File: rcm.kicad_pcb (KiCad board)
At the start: 2 copper layers, 140 x 70 mm, 159 parts, among them Y1 8MHz, Y2 32.768kHz

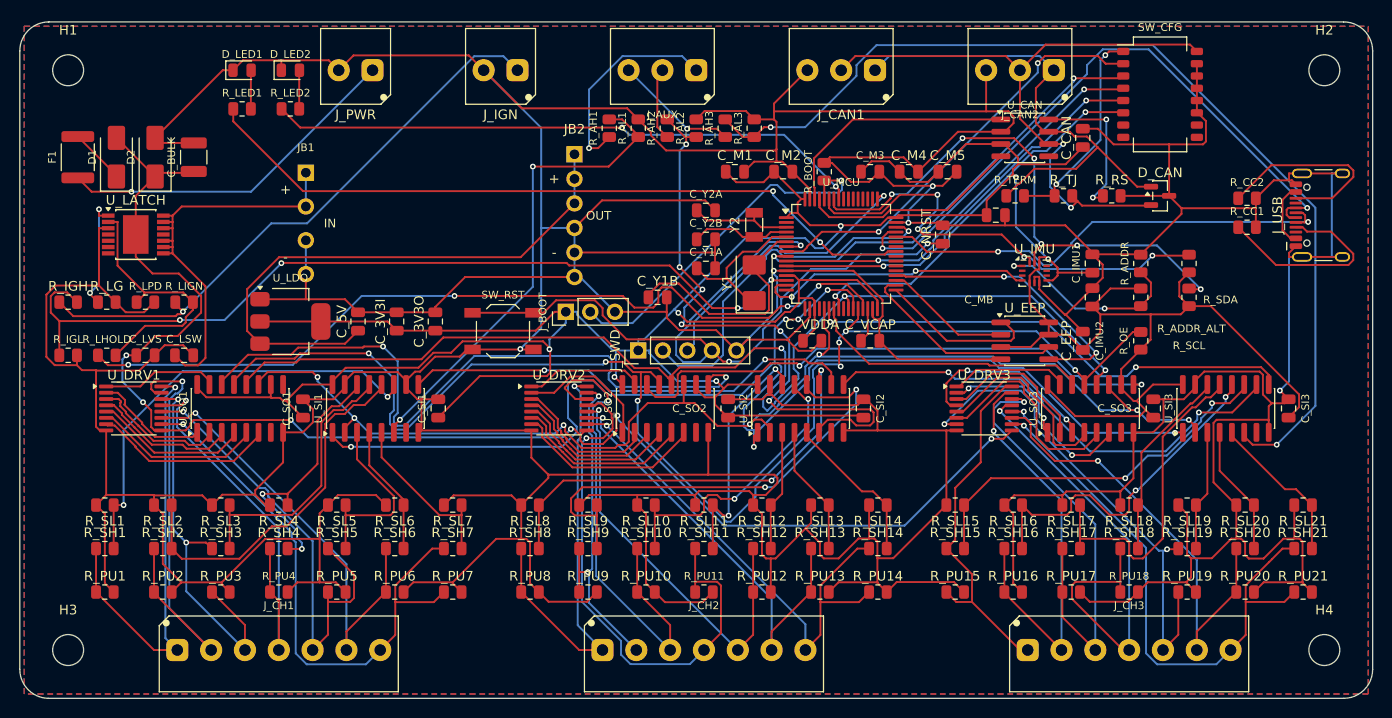
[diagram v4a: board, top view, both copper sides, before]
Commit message: rcm: apply the GND-to-pour version for review (NOT orderable)
Applied rcm_noroute to rcm.kicad_pcb so it can be looked at. Good board
is in git and at rcm.kicad_pcb.bak_gnd_routed; mfg/ still matches the
GOOD board, not what is on disk.

  good      426/426 routed, 2078 segments, 166 vias, 0 unconnected
  this      293/293 routed, 1605 segments (-23%), 165 vias, 25 unconnected

Electrical DRC is clean on both. What remains here is 8 GND pads the pour
cannot reach - five of them MCU grounds - plus pour-island-to-island
items.

Fixes to stitch_zone_vias.py, all found by running the FULL DRC on the
first attempt rather than only checking connectivity:

  - rescue traces were checked against pads but never against TRACKS, so
    one drove through SR_SCK and shorted it
  - hand-rolled clearance missed hole-to-hole against THT pads; a via
    landed 0.077mm from the battery input
  - stitching was a blanket 4mm grid, 250 vias, most joining the main
    pour to itself for nothing while perforating it

Now stitches only genuine islands (largest filled polygon is the main
pour and is skipped), and validates every placement with the real KiCad
DRC instead of my own arithmetic.

Co-Authored-By: Claude Opus 5 <noreply@anthropic.com>
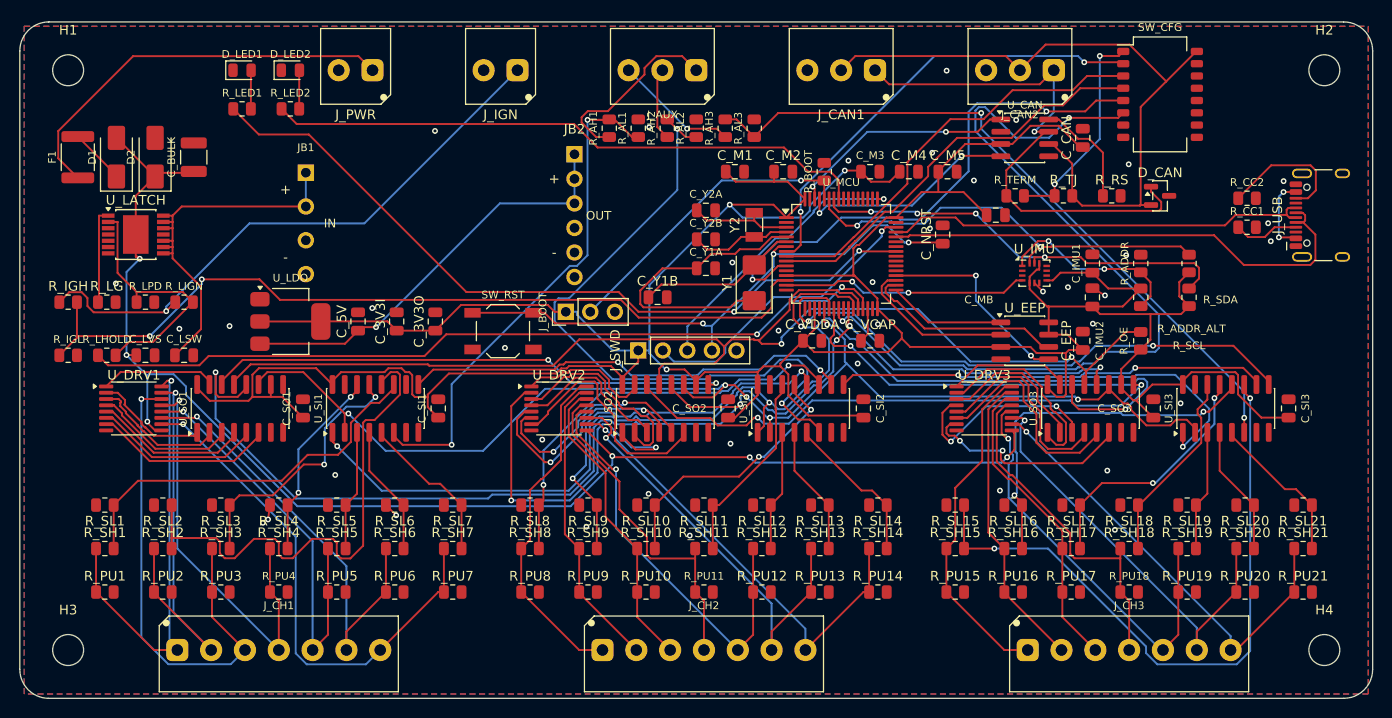
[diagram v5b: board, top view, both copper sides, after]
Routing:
- net GND: track 1068.3 -> 5.75 mm, vias 5 -> 40
- net CFG_IMU_EN: track 39.8 -> 87.8 mm
- net ASNS3: track 103.7 -> 72.6 mm
- net SNS15: track 39.3 -> 67.9 mm
- net NRST: track 83.9 -> 59.4 mm
- net DRV9: track 14.3 -> 38.8 mm, vias 0 -> 2
- net USB_DP: track 66.4 -> 44.5 mm, vias 2 -> 0
- net SR_MOSI: track 29.3 -> 50.0 mm, vias 0 -> 2
- net CH11: track 56.4 -> 35.7 mm, vias 1 -> 0
- net CH10: track 51.0 -> 31.5 mm, vias 1 -> 0
- net SR_RCLK: track 118.2 -> 135.4 mm, vias 3 -> 5
- net SR_CH21: track 70.8 -> 54.3 mm
- net +5V: track 59.5 -> 43.6 mm, vias 0 -> 1
- net SNS2: track 38.2 -> 53.7 mm
- net HSE_IN: track 16.0 -> 31.0 mm
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
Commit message: rcm: keep MCU grounds routed, rest to the pour - 8 isolated pads -> 3
route_board.py gains --no-route-keep: a reference prefix whose pins stay
in the --no-route net. Keeping U_MCU's 5 ground pins in the netlist while
handing the other 131 to the pour fixes the failure mode outright.

  good board          2078 segments, 166 vias, 0 unconnected
  GND fully to pour   1605 segments, 165 vias, 8 isolated pads (5 MCU gnd)
  GND except MCU      1574 segments, 208 vias, 3 isolated pads (no MCU gnd)

The MCU's grounds are boxed in by its own escape routing so the pour was
never going to reach them, but they are trivial for the router once back
in the netlist - and it cost nothing in copper (1574 vs 1605 segments).

Electrical DRC is 0 on all three. Remaining 3: U_LATCH.3, U_SI1.15,
U_SI2.15 - shift registers with the same problem one level down, and the
obvious next step is adding them to --no-route-keep.

Applied to rcm.kicad_pcb for review; NOT orderable. Good board at
rcm.kicad_pcb.bak_gnd_routed, and mfg/ still matches THAT, not this.

Co-Authored-By: Claude Opus 5 <noreply@anthropic.com>
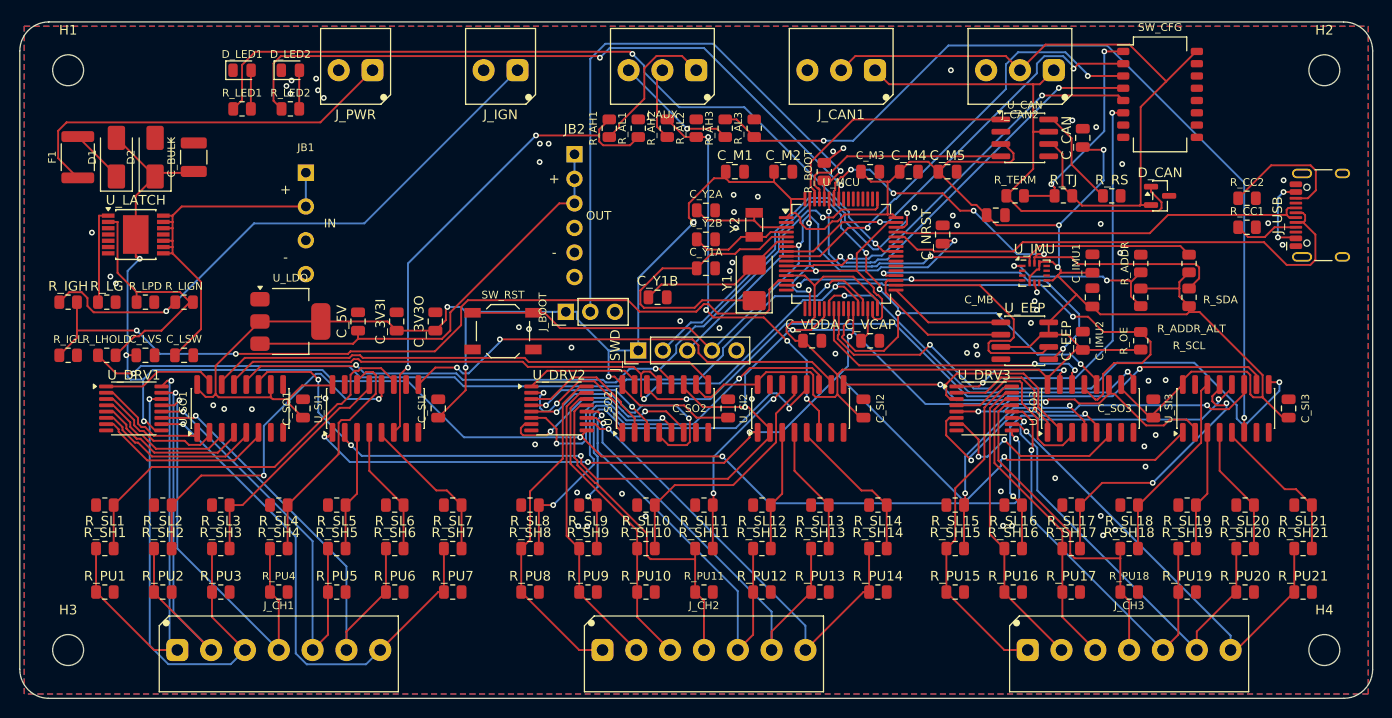
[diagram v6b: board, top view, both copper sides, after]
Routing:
- net GND: track 5.75 -> 41.3 mm, vias 40 -> 71
- net BOOT0: track 31.8 -> 62.2 mm
- net CFG_IMU_EN: track 87.8 -> 61.4 mm
- net ASNS2: track 69.4 -> 43.5 mm, vias 2 -> 4
- net SR_PL: track 137.6 -> 112.2 mm, vias 4 -> 5
- net SNS15: track 67.9 -> 42.8 mm
- net DRV9: track 38.8 -> 16.5 mm
- net SR_MOSI: track 50.0 -> 31.3 mm
- net ASNS3: track 72.6 -> 90.4 mm
- net SNS2: track 53.7 -> 37.3 mm, vias 0 -> 2
- net CFG_BAUD: track 55.4 -> 42.6 mm
- net +3V3: track 389.4 -> 376.8 mm, vias 3 -> 7
- net SR_SCK: track 128.7 -> 140.0 mm
- net SR_RCLK: track 135.4 -> 124.9 mm, vias 5 -> 6
- net LED2: track 62.7 -> 72.0 mm, vias 0 -> 2
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
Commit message: rcm: add 4-layer variant rcm4.kicad_pcb, routed the normal way
Built as a parallel variant with GND routed normally and the inner layers
as planes - F.Cu / GND_plane / PWR_plane(+3V3) / B.Cu. Drops the
--no-route experimentation entirely.

  2-layer  426/426, 0 unconnected, 0 parity, 2078 segments, 166 vias
  4-layer  426/426, 0 unconnected, 0 parity, 2148 segments, 164 vias

Both electrically clean. The 4-layer is not less copper - it is a
continuous ground reference under every trace instead of whatever pour
fragment is nearby, which is the actual argument for CAN, USB and a
crystal on a board switching inductive loads. It also routed first time
without fighting, which the 2-layer did not.

Before ordering it needs a stackup block (the pdm14-revB trap), a
re-quote, and fresh gerbers - mfg/ is still the 2-layer board. The layer
count and plane zones were applied by hand to a fresh netlist_to_board
output rather than generated, so a schematic change means redoing that.

2-layer board and mfg/ are untouched and remain the orderable set.

Co-Authored-By: Claude Opus 5 <noreply@anthropic.com>
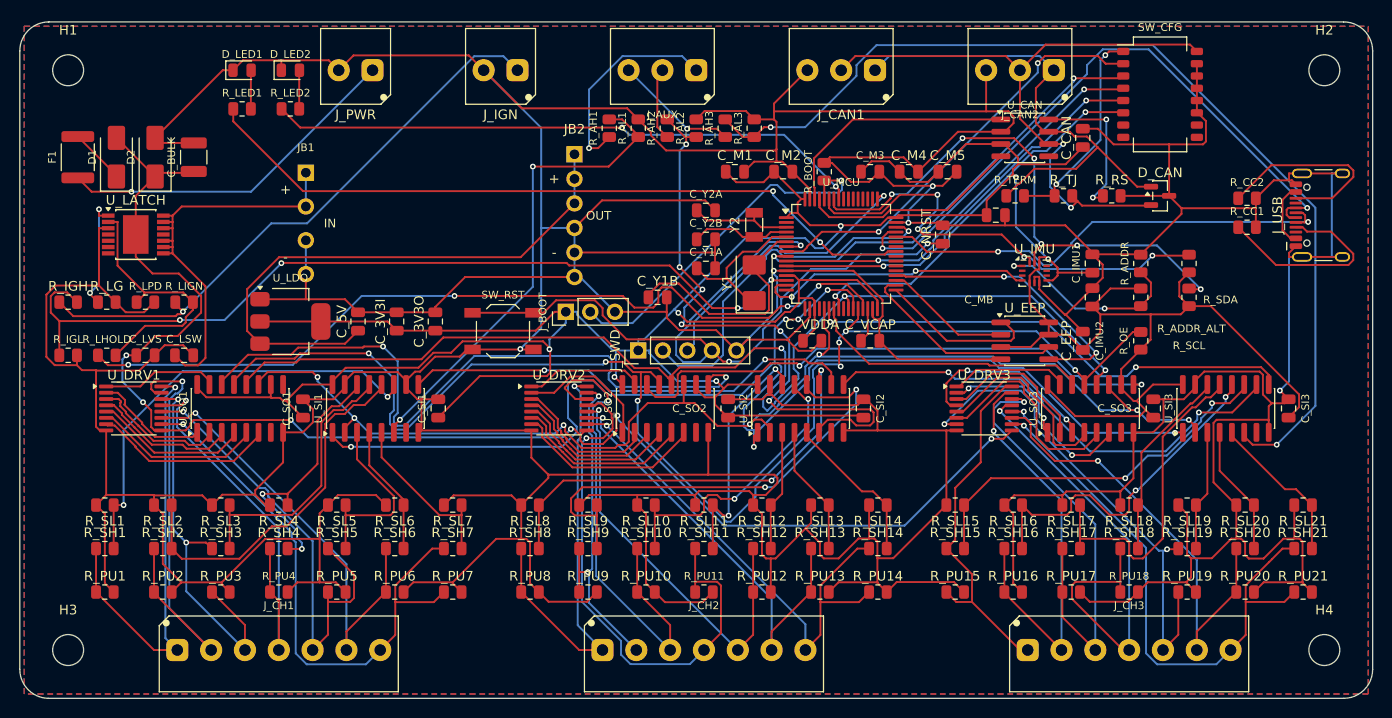
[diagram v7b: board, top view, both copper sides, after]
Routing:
- net GND: track 41.3 -> 1068.3 mm, vias 71 -> 5
- net BOOT0: track 62.2 -> 37.6 mm
- net SR_PL: track 112.2 -> 135.0 mm, vias 5 -> 6
- net USB_DP: track 43.9 -> 66.4 mm, vias 0 -> 2
- net CFG_IMU_EN: track 61.4 -> 39.8 mm
- net CH11: track 35.7 -> 56.4 mm, vias 0 -> 1
- net ASNS2: track 43.5 -> 63.4 mm, vias 4 -> 6
- net CH10: track 31.4 -> 51.0 mm, vias 0 -> 1
- net SR_CH21: track 53.3 -> 70.8 mm, vias 0 -> 2
- net NRST: track 67.5 -> 83.9 mm, vias 2 -> 3
- net SR_OE_N: track 125.4 -> 140.7 mm, vias 3 -> 7
- net CH18: track 35.7 -> 50.9 mm, vias 0 -> 1
- net HSE_IN: track 31.1 -> 16.0 mm
- net USB_CC1: track 6.81 -> 21.5 mm
- net CH17: track 31.5 -> 46.1 mm, vias 0 -> 1
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
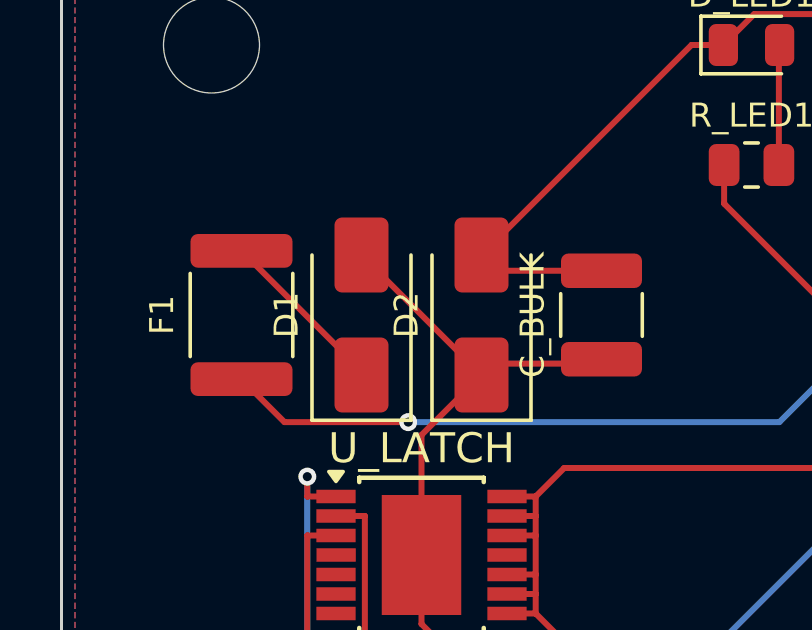
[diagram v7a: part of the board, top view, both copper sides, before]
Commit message: rcm: D1 corrected in place on both boards - no re-route needed
The netlist fix swapped which net each of D1's two pads carries. Because
D_SMA's pads are symmetric about the footprint origin, rotating the part
180 degrees lands pad 1 exactly where pad 2 was - so rotating AND
reassigning the nets together lets the existing traces arrive at the
right pads with no routing changed at all. That matters on rcm4, where
the routing has been hand-tidied and is not reproducible from a rebuild.

Both boards verified electrically rather than just DRC-clean:

  rcm4   pad2 (A) = +12V_FUSED, pad1 (K) = +12V_P
  rcm    pad2 (A) = +12V_FUSED, pad1 (K) = +12V_P

Current flows fuse -> anode -> cathode -> protected rail on both. The two
carry different D1 rotations, which is fine; both are correct.

0 unconnected, 0 schematic parity, 0 electrical violations on both. The
schematic-parity result is the real confirmation - it means each board
now matches the corrected netlist.

Manufacturing files are still stale on both and need regenerating, but
neither board needs re-routing.

Co-Authored-By: Claude Opus 5 <noreply@anthropic.com>
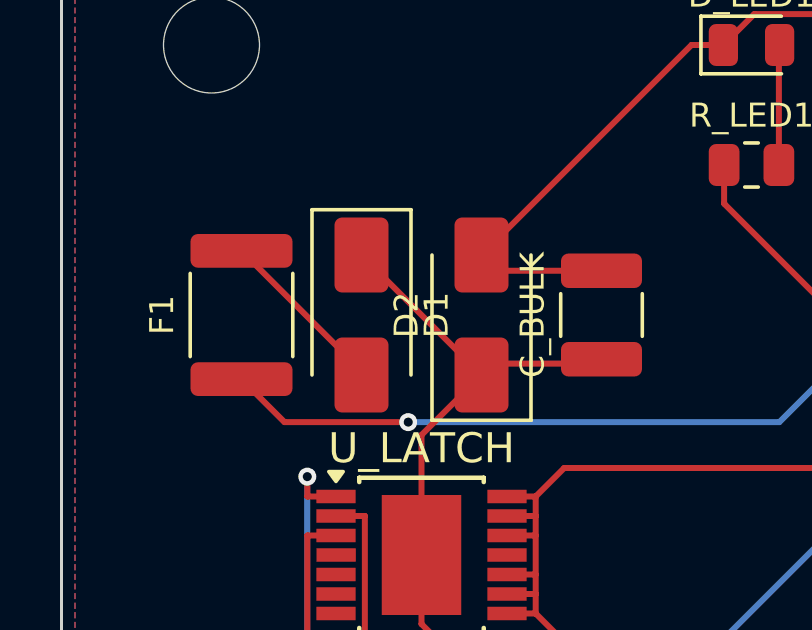
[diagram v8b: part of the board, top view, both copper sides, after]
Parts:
- turned D1 to -90 degrees
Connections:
- D1 pad 1: +12V_FUSED -> +12V_P
- D1 pad 2: +12V_P -> +12V_FUSED
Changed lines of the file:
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@@
 		(tags "capacitor")
 		(property "Reference" "C_MB"
-			(at -1.750 8.750 0)
+			(at -1.75 8.75 0)
 			(layer "F.SilkS")
 			(effects
@@
 		(tags "resistor")
 		(property "Reference" "R_OE"
-			(at -0.000 -1.750 90)
+			(at 0 -1.75 90)
 			(layer "F.SilkS")
 			(effects
@@
 		(tags "capacitor")
 		(property "Reference" "C_IMU2"
-			(at -4.500 0.750 90)
+			(at -4.5 0.75 90)
 			(layer "F.SilkS")
 			(effects
@@
 		(tags "capacitor")
 		(property "Reference" "C_SI2"
-			(at 0.000 1.750 90)
+			(at 0 1.75 90)
 			(layer "F.SilkS")
 			(effects
@@
 	(footprint "Diode_SMD:D_SMA"
 		(layer "F.Cu")
-		(at 10 14 90)
+		(at 10 14 -90)
 		(descr "Diode SMA (DO-214AC)")
 		(tags "Diode SMA (DO-214AC)")
 		(property "Reference" "D1"
-			(at 0 -2.5 90)
+			(at 0 -2.5 270)
 			(layer "F.SilkS")
 			(effects
@@
 		)
 		(property "Value" "SS34"
-			(at 0 2.6 90)
+			(at 0 2.6 270)
 			(layer "F.Fab")
 			(effects
@@
 		)
 		(property "Datasheet" ""
-			(at 0 0 90)
+			(at 0 0 270)
 			(unlocked yes)
 			(layer "F.Fab")
@@
 		)
 		(property "Description" ""
-			(at 0 0 90)
+			(at 0 0 270)
 			(unlocked yes)
 			(layer "F.Fab")
@@
 		(duplicate_pad_numbers_are_jumpers no)
 		(fp_line
-			(start -3.51 -1.65)
-			(end 2 -1.65)
+			(start -3.51 1.65)
+			(end 2 1.65)
 			(stroke
 				(width 0.12)
@@
 		)
 		(fp_line
-			(start -3.51 1.65)
-			(end 2 1.65)
+			(start -3.51 -1.65)
+			(end 2 -1.65)
 			(stroke
 				(width 0.12)
@@
 		)
 		(fp_line
-			(start 3.5 -1.75)
-			(end 3.5 1.75)
+			(start -3.5 1.75)
+			(end -3.5 -1.75)
 			(stroke
 				(width 0.05)
@@
 		)
 		(fp_line
-			(start -3.5 -1.75)
-			(end 3.5 -1.75)
+			(start 3.5 1.75)
+			(end -3.5 1.75)
 			(stroke
 				(width 0.05)
@@
 		)
 		(fp_line
-			(start 3.5 1.75)
-			(end -3.5 1.75)
+			(start -3.5 -1.75)
+			(end 3.5 -1.75)
 			(stroke
 				(width 0.05)
@@
 		)
 		(fp_line
-			(start -3.5 1.75)
-			(end -3.5 -1.75)
+			(start 3.5 -1.75)
+			(end 3.5 1.75)
 			(stroke
 				(width 0.05)
@@
 		)
 		(fp_line
-			(start 2.3 -1.5)
+			(start -2.3 1.5)
 			(end -2.3 -1.5)
 			(stroke
@@
 		)
 		(fp_line
-			(start 2.3 -1.5)
-			(end 2.3 1.5)
+			(start 2.3 1.5)
+			(end -2.3 1.5)
 			(stroke
 				(width 0.1)
@@
 		)
 		(fp_line
-			(start -0.64944 -0.79908)
-			(end -0.64944 0.80112)
+			(start 0.50118 0.75032)
+			(end 0.50118 -0.79908)
 			(stroke
 				(width 0.1)
@@
 		)
 		(fp_line
-			(start 0.50118 0.00102)
-			(end 1.4994 0.00102)
+			(start -0.64944 0.00102)
+			(end 0.50118 0.75032)
 			(stroke
 				(width 0.1)
@@
 		(fp_line
 			(start -0.64944 0.00102)
-			(end 0.50118 -0.79908)
+			(end -1.55114 0.00102)
 			(stroke
 				(width 0.1)
@@
 		(fp_line
 			(start -0.64944 0.00102)
-			(end -1.55114 0.00102)
+			(end 0.50118 -0.79908)
 			(stroke
 				(width 0.1)
@@
 		)
 		(fp_line
-			(start -0.64944 0.00102)
-			(end 0.50118 0.75032)
+			(start 0.50118 0.00102)
+			(end 1.4994 0.00102)
 			(stroke
 				(width 0.1)
@@
 		)
 		(fp_line
-			(start 0.50118 0.75032)
-			(end 0.50118 -0.79908)
+			(start -0.64944 -0.79908)
+			(end -0.64944 0.80112)
 			(stroke
 				(width 0.1)
@@
 		)
 		(fp_line
-			(start 2.3 1.5)
-			(end -2.3 1.5)
+			(start 2.3 -1.5)
+			(end 2.3 1.5)
 			(stroke
 				(width 0.1)
@@
 		)
 		(fp_line
-			(start -2.3 1.5)
+			(start 2.3 -1.5)
 			(end -2.3 -1.5)
 			(stroke
@@
 		)
 		(fp_text user "${REFERENCE}"
-			(at 0 -2.5 90)
+			(at 0 -2.5 270)
 			(layer "F.Fab")
 			(effects
@@
 		)
 		(pad "1" smd roundrect
-			(at -2 0 90)
+			(at -2 0 270)
 			(size 2.5 1.8)
 			(layers "F.Cu" "F.Mask" "F.Paste")
 			(roundrect_rratio 0.1388888889)
-			(net "+12V_FUSED")
+			(net "+12V_P")
 		)
 		(pad "2" smd roundrect
-			(at 2 0 90)
+			(at 2 0 270)
 			(size 2.5 1.8)
 			(layers "F.Cu" "F.Mask" "F.Paste")
 			(roundrect_rratio 0.1388888889)
-			(net "+12V_P")
+			(net "+12V_FUSED")
 		)
 		(embedded_fonts no)
@@
 		(tags "capacitor")
 		(property "Reference" "C_SO2"
-			(at -0.000 -4.000 0)
+			(at 0 -4 0)
 			(layer "F.SilkS")
 			(effects
@@
 		(tags "capacitor")
 		(property "Reference" "C_SO3"
-			(at -0.000 -4.000 0)
+			(at 0 -4 0)
 			(layer "F.SilkS")
 			(effects
@@
 		(tags "resistor")
 		(property "Reference" "R_SCL"
-			(at -5.000 0.000 0)
+			(at -5 0 0)
 			(layer "F.SilkS")
 			(effects
@@
 		(tags "resistor")
 		(property "Reference" "R_SDA"
-			(at -3.750 3.250 0)
+			(at -3.75 3.25 0)
 			(layer "F.SilkS")
 			(effects
@@
 		(tags "resistor")
 		(property "Reference" "R_ADDR_ALT"
-			(at -3.250 5.250 0)
+			(at -3.25 5.25 0)
 			(layer "F.SilkS")
 			(effects
@@
 		(tags "capacitor")
 		(property "Reference" "C_SI3"
-			(at 0.000 1.750 90)
+			(at 0 1.75 90)
 			(layer "F.SilkS")
 			(effects
